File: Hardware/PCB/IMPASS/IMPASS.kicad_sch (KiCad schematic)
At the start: 0 parts

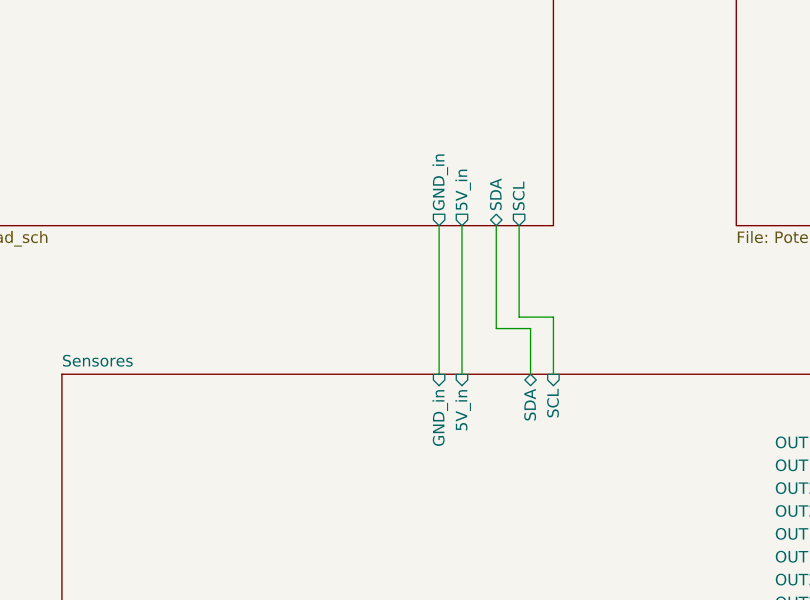
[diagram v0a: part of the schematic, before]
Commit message: Schematics: Added mpu6050
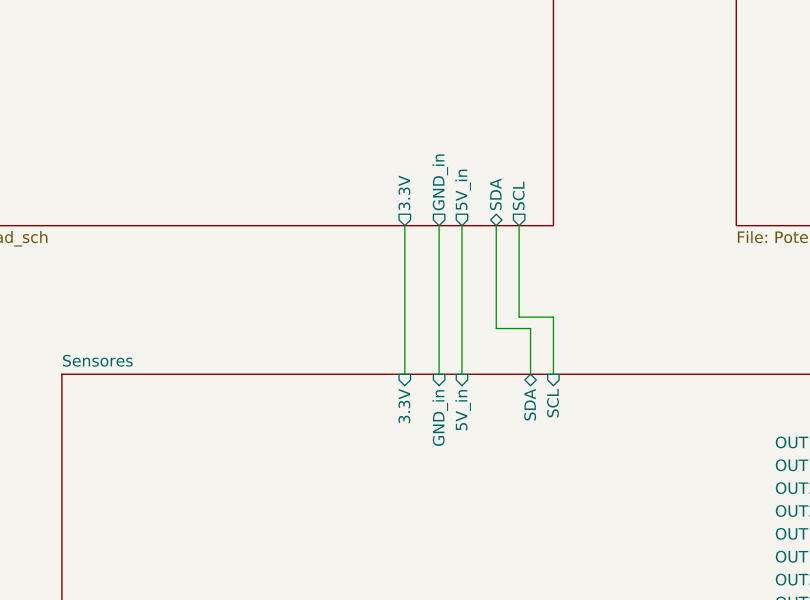
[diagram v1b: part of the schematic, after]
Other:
- sheet Logica ports: added 3.3V; removed none
- sheet Sensores ports: added 3.3V; removed none
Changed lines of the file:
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@@
+	(wire
+		(pts
+			(xy 91.44 106.68) (xy 91.44 123.19)
+		)
+		(stroke
+			(width 0)
+			(type default)
+		)
+	)
 	(wire
 		(pts
@@
 			)
 		)
+		(pin "3.3V" output
+			(at 91.44 106.68 270)
+			(effects
+				(font
+					(size 1.27 1.27)
+				)
+				(justify left)
+			)
+		)
 		(instances
 			(project "IMPASS"
@@
 			(effects
 				(font
+					(size 1.27 1.27)
+				)
+				(justify right)
+			)
+		)
+		(pin "3.3V" input
+			(at 91.44 123.19 90)
+			(effects
+				(font

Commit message: Update to v1
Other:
- sheet Logica ports: added ADC1, ADC2, ADC3, ADC4, ADC5, ADC6, CS_ADC, CS_INCL, MISO, MOSI, SCK; removed none
- sheet Sensores ports: added ADC1, ADC2, ADC3, ADC4, ADC5, ADC6, CS_ADC, CS_INCL, MISO, MOSI, SCK; removed none

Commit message: Update v1
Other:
- company: (none) -> Luis Miguel Carmona Cortés
- title: (none) -> IMPASS 
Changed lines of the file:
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@@
 	(generator_version "8.0")
 	(paper "A4")
+	(title_block
+		(title "IMPASS ")
+		(date "2026-01-12")
+		(rev "v1.0")
+		(company "Luis Miguel Carmona Cortés")
+		(comment 1 "Bloques globales")
+	)
 	(wire
 		(pts
